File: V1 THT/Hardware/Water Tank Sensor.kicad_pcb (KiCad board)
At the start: 2 copper layers, 47 x 58 mm, 21 parts, among them J1 Programming port, J2 Temp Sensor, J3 Water Level, J4 Valve Terminal, J5 12v In, Q1 2N3904, U1 WeMos_D1_mini

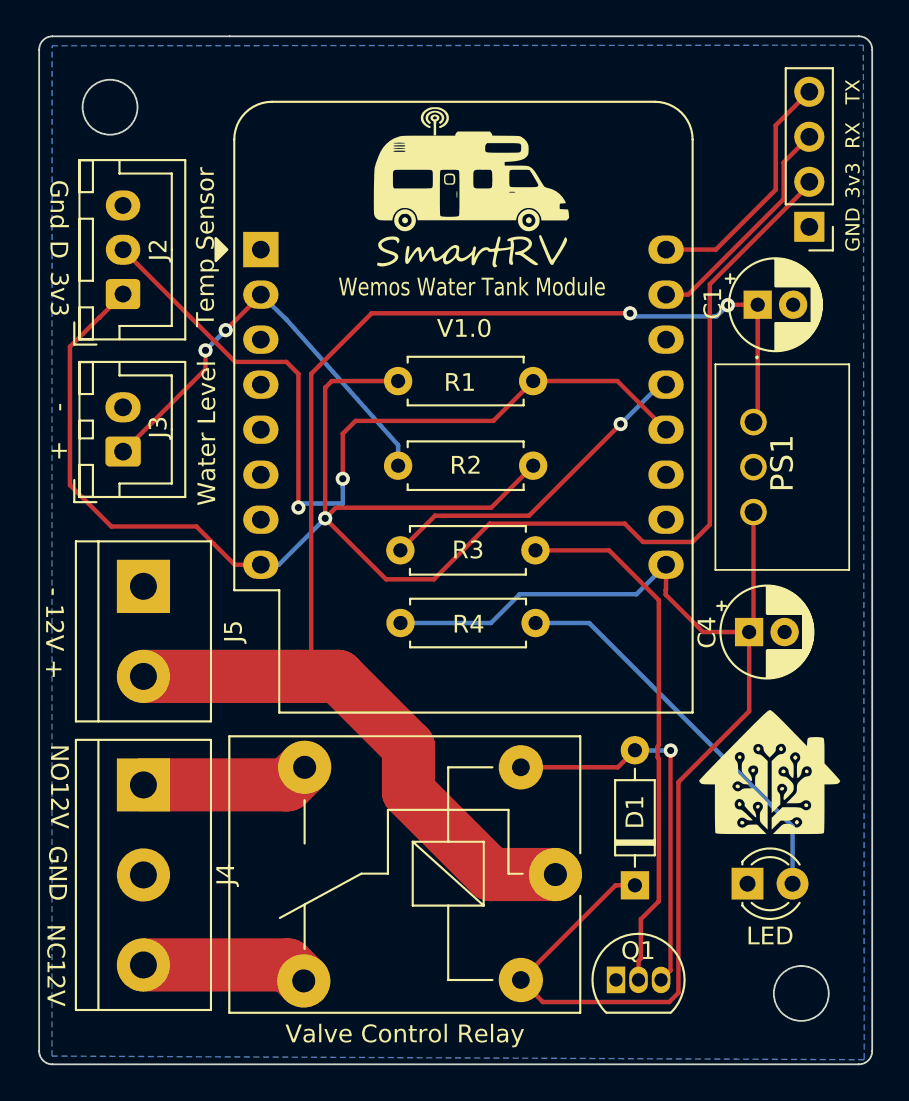
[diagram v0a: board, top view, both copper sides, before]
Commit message: Updated files to v1.1 incnluding images annotating resistor to vary depending on ADC sensor.
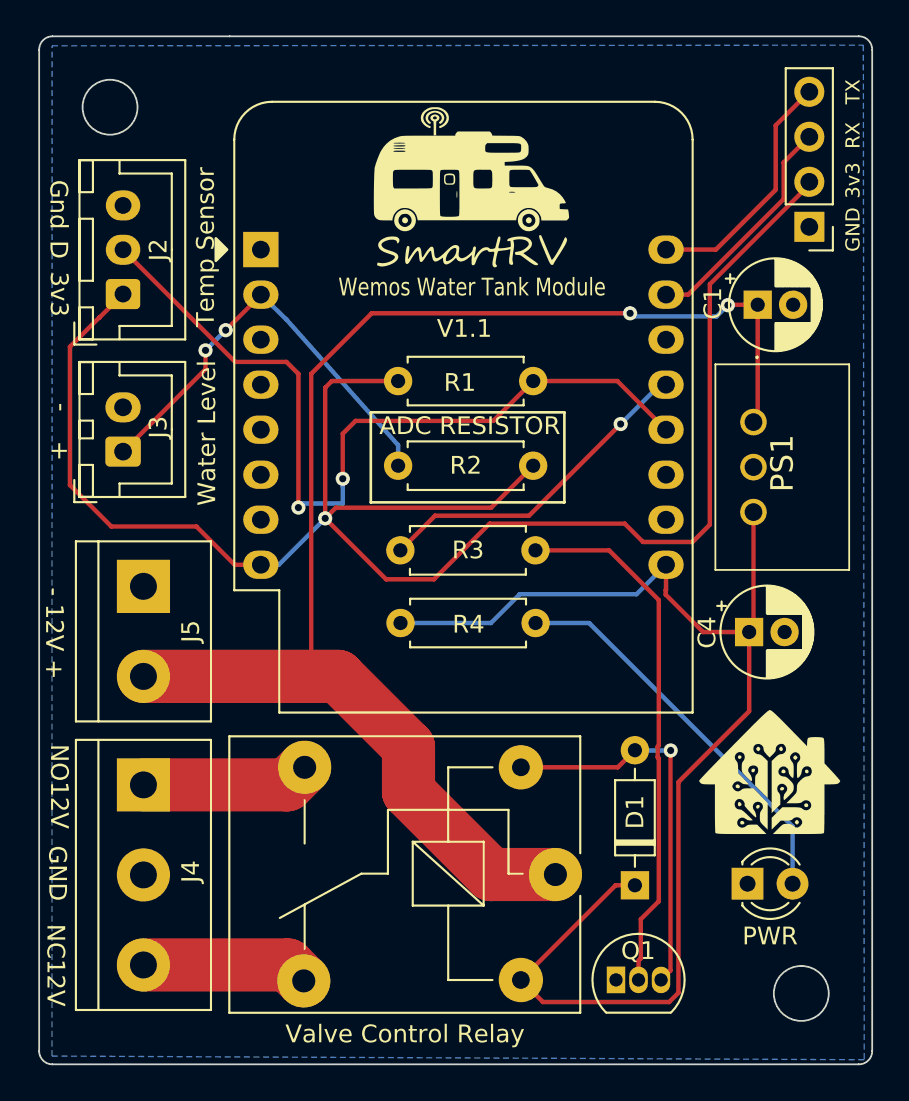
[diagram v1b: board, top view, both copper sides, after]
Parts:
- D2: value LED -> PWR
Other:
- board text added: "ADC RESISTOR"
- board text added: "V1.1"
- board text removed: "V1.0"

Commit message: Updated v1.2
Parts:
- removed the G*** at (131.2, 81.6)
- removed REF**: KiCad-Logo2_6mm_SilkScreen, Symbol:KiCad-Logo2_6mm_SilkScreen
- added D3: 1N4148, Diode_THT:D_DO-35_SOD27_P7.62mm_Horizontal, F.Cu at (117.9, 55.6)
- added D4: Relay, LED_THT:LED_D3.0mm, F.Cu at (131.7, 90.0)
- added G***: LOGO, logos:githubqr, B.Cu at (111.2, 87.5)
- added R5: 10k, Resistor_THT:R_Axial_DIN0207_L6.3mm_D2.5mm_P7.62mm_Horizontal, F.Cu at (118.0, 76.7)
- D2: value PWR -> Power LED
- J1: footprint Connector_PinHeader_2.54mm:PinHeader_1x04_P2.54mm_Vertical -> Connector_PinSocket_2.54mm:PinSocket_1x04_P2.54mm_Vertical
- J4: footprint TerminalBlock:TerminalBlock_bornier-3_P5.08mm -> TerminalBlock_Phoenix:TerminalBlock_Phoenix_PT-1,5-3-5.0-H_1x03_P5.00mm_Horizontal
- J5: footprint TerminalBlock:TerminalBlock_bornier-2_P5.08mm -> TerminalBlock_Phoenix:TerminalBlock_Phoenix_PT-1,5-2-5.0-H_1x02_P5.00mm_Horizontal
- Relay1: renamed from Valve Control Relay
- moved D2 4.51 mm to (131.7, 83.7), turned to 90 degrees
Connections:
- C1 pad 1: +12V -> Net-(C1-Pad1)
- PS1 pad 1: +12V -> Net-(C1-Pad1)
- Q1 pad 1: GND -> Net-(Q1-Pad1)
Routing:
- net +12V: track 80.4 -> 51.5 mm, vias 2 -> 0
- net Net-(Q1-Pad1): track 0.00 -> 24.6 mm
- net Net-(D4-Pad2): track 0.00 -> 21.5 mm
- net Net-(C1-Pad1): track 0.00 -> 19.8 mm, vias 0 -> 2
- net Net-(D2-Pad2): track 22.5 -> 17.0 mm
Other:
- outline, holes or cut-outs redrawn
- board text added: "Github"
- board text added: "V1.2"
- board text added: "Water Tank Module"
- board text removed: "V1.1"
- board text removed: "Wemos Water Tank Module"

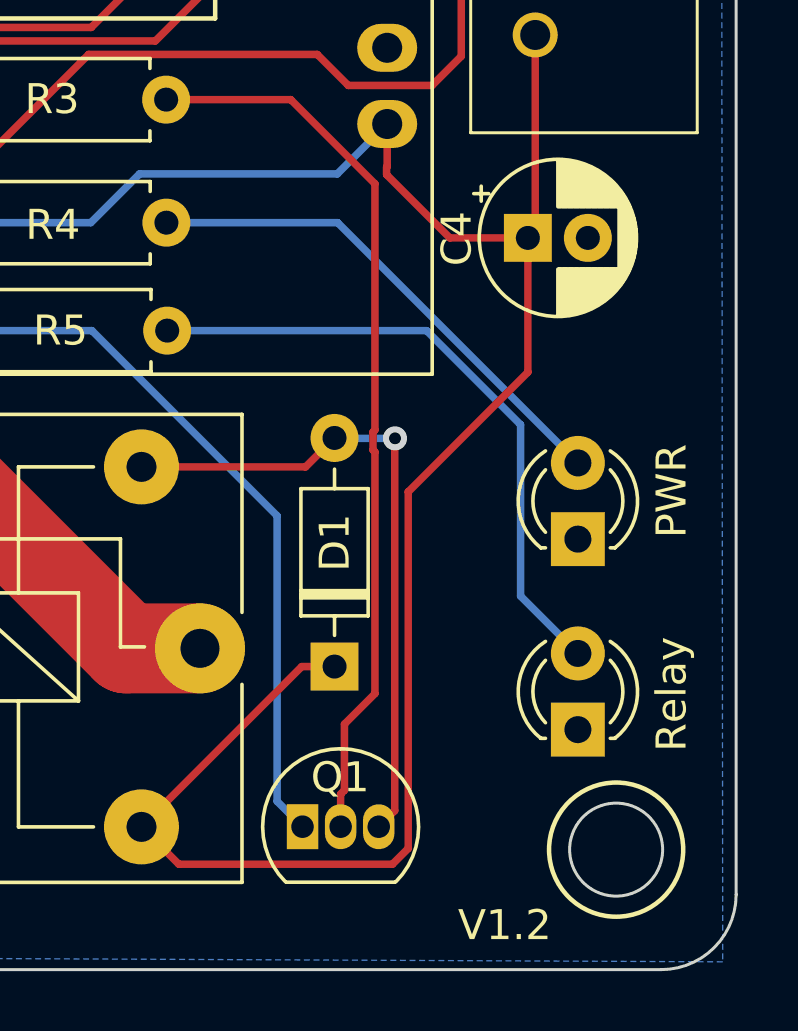
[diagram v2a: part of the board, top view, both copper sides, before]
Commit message: Updated V1 THT to V1.3
THT version updated to final model with revisions. No further changes will be made to V1. Boards available to purchase from store
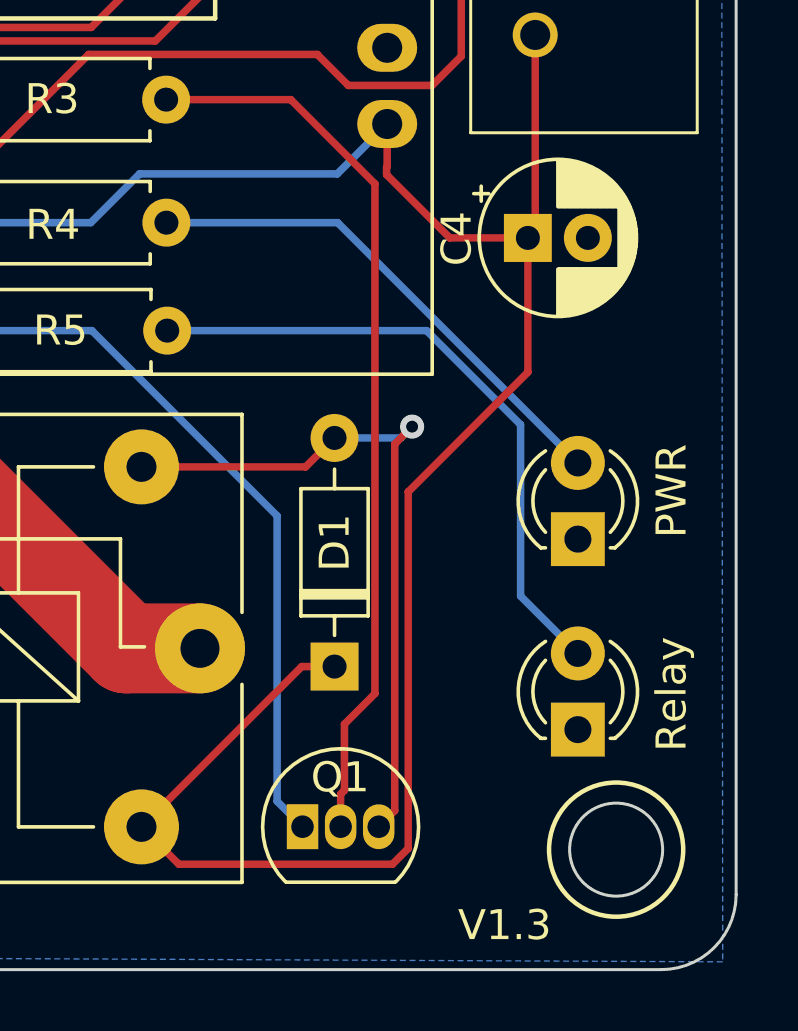
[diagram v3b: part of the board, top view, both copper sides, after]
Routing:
- net Net-(D1-Pad2): track 22.0 -> 23.4 mm
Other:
- board text added: "V1.3"
- board text removed: "V1.2"
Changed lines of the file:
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@@
     (effects (font (size 1 1) (thickness 0.25)))
   )
-  (gr_text "V1.2" (at 129.286 96.52) (layer "F.SilkS")
+  (gr_text "V1.3" (at 129.286 96.52) (layer "F.SilkS")
     (effects (font (size 1 1) (thickness 0.15)))
   )
@@
   (segment (start 115.4891 73.1012) (end 110.3884 73.1012) (width 0.25) (layer "B.Cu") (net 10))
   (segment (start 123.7056 71.4756) (end 117.1147 71.4756) (width 0.25) (layer "B.Cu") (net 10))
+  (segment (start 125.62 80.48) (end 125.62 92.7026) (width 0.25) (layer "F.Cu") (net 11))
+  (segment (start 126.2 79.9) (end 125.62 80.48) (width 0.25) (layer "F.Cu") (net 11))
+  (segment (start 117.1784 81.2418) (end 122.6492 81.2418) (width 0.25) (layer "F.Cu") (net 11))
   (segment (start 125.62 92.7026) (end 125.0866 93.236) (width 0.25) (layer "F.Cu") (net 11))
-  (segment (start 125.62 80.300815) (end 125.62 92.7026) (width 0.25) (layer "F.Cu") (net 11))
-  (segment (start 117.1784 81.2418) (end 122.6492 81.2418) (width 0.25) (layer "F.Cu") (net 11))
   (segment (start 122.6492 81.2418) (end 123.6134 80.2776) (width 0.25) (layer "F.Cu") (net 11))
-  (segment (start 125.629357 80.291458) (end 125.62 80.300815) (width 0.25) (layer "F.Cu") (net 11))
-  (via (at 125.629357 80.291458) (size 0.8) (drill 0.4) (layers "F.Cu" "B.Cu") (net 11))
-  (segment (start 123.627258 80.291458) (end 123.6134 80.2776) (width 0.25) (layer "B.Cu") (net 11))
-  (segment (start 125.629357 80.291458) (end 123.627258 80.291458) (width 0.25) (layer "B.Cu") (net 11))
+  (via (at 126.2 79.9) (size 0.8) (drill 0.4) (layers "F.Cu" "B.Cu") (net 11))
+  (segment (start 126.2 79.9) (end 125.8224 80.2776) (width 0.25) (layer "B.Cu") (net 11))
+  (segment (start 125.8224 80.2776) (end 123.6134 80.2776) (width 0.25) (layer "B.Cu") (net 11))
   (segment (start 133.4516 48.375318) (end 133.4516 48.2092) (width 0.25) (layer "F.Cu") (net 12))
   (segment (start 91.7364 65.317) (end 94.0732 67.6538) (width 0.25) (layer "F.Cu") (net 12))
@@
   (segment (start 95.8836 92.3934) (end 104.03 92.3934) (width 3) (layer "F.Cu") (net 17))
   (segment (start 103.9284 92.2918) (end 104.9284 93.2918) (width 0.25) (layer "F.Cu") (net 17))
+  (segment (start 124.95974 71.80414) (end 122.1556 69) (width 0.25) (layer "F.Cu") (net 18))
+  (segment (start 123.8166 93.236) (end 123.8166 92.14968) (width 0.25) (layer "F.Cu") (net 18))
+  (segment (start 123.8166 92.14968) (end 123.94374 92.02254) (width 0.25) (layer "F.Cu") (net 18))
+  (segment (start 124.95974 88.800282) (end 124.95974 71.80414) (width 0.25) (layer "F.Cu") (net 18))
+  (segment (start 122.1556 69) (end 118 69) (width 0.25) (layer "F.Cu") (net 18))
   (segment (start 123.94374 89.816282) (end 124.95974 88.800282) (width 0.25) (layer "F.Cu") (net 18))
-  (segment (start 124.895489 80.079097) (end 124.95974 80.014846) (width 0.25) (layer "F.Cu") (net 18))
-  (segment (start 124.95974 80.743554) (end 124.895489 80.679303) (width 0.25) (layer "F.Cu") (net 18))
   (segment (start 123.94374 92.02254) (end 123.94374 89.816282) (width 0.25) (layer "F.Cu") (net 18))
-  (segment (start 124.95974 80.014846) (end 124.95974 71.80414) (width 0.25) (layer "F.Cu") (net 18))
-  (segment (start 124.895489 80.679303) (end 124.895489 80.079097) (width 0.25) (layer "F.Cu") (net 18))
-  (segment (start 124.95974 71.80414) (end 122.1556 69) (width 0.25) (layer "F.Cu") (net 18))
-  (segment (start 123.8166 92.14968) (end 123.94374 92.02254) (width 0.25) (layer "F.Cu") (net 18))
-  (segment (start 122.1556 69) (end 118 69) (width 0.25) (layer "F.Cu") (net 18))
-  (segment (start 124.95974 88.800282) (end 124.95974 80.743554) (width 0.25) (layer "F.Cu") (net 18))
-  (segment (start 123.8166 93.236) (end 123.8166 92.14968) (width 0.25) (layer "F.Cu") (net 18))
   (segment (start 110.38 69) (end 112.3358 67.0442) (width 0.25) (layer "F.Cu") (net 19))
   (segment (start 112.3358 67.0442) (end 117.6392 67.0442) (width 0.25) (layer "F.Cu") (net 19))
@@
     (connect_pads (clearance 0))
     (min_thickness 0.254)
-    (keepout (tracks not_allowed) (vias not_allowed) (pads not_allowed ) (copperpour not_allowed) (footprints allowed))
+    (keepout (tracks not_allowed) (vias not_allowed) (pads not_allowed) (copperpour not_allowed) (footprints allowed))
     (fill (thermal_gap 0.508) (thermal_bridge_width 0.508))
     (polygon
